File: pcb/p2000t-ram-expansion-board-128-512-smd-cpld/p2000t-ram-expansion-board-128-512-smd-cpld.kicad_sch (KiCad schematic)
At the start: 19 parts, among them J1 EXPANSION BOARD, J2 POWER, J3 TERMINAL, J4 Atmel-JTAG-10, U1 ATF1502ASV, U2 62128, U3 62128, U4 62128, U5 62128

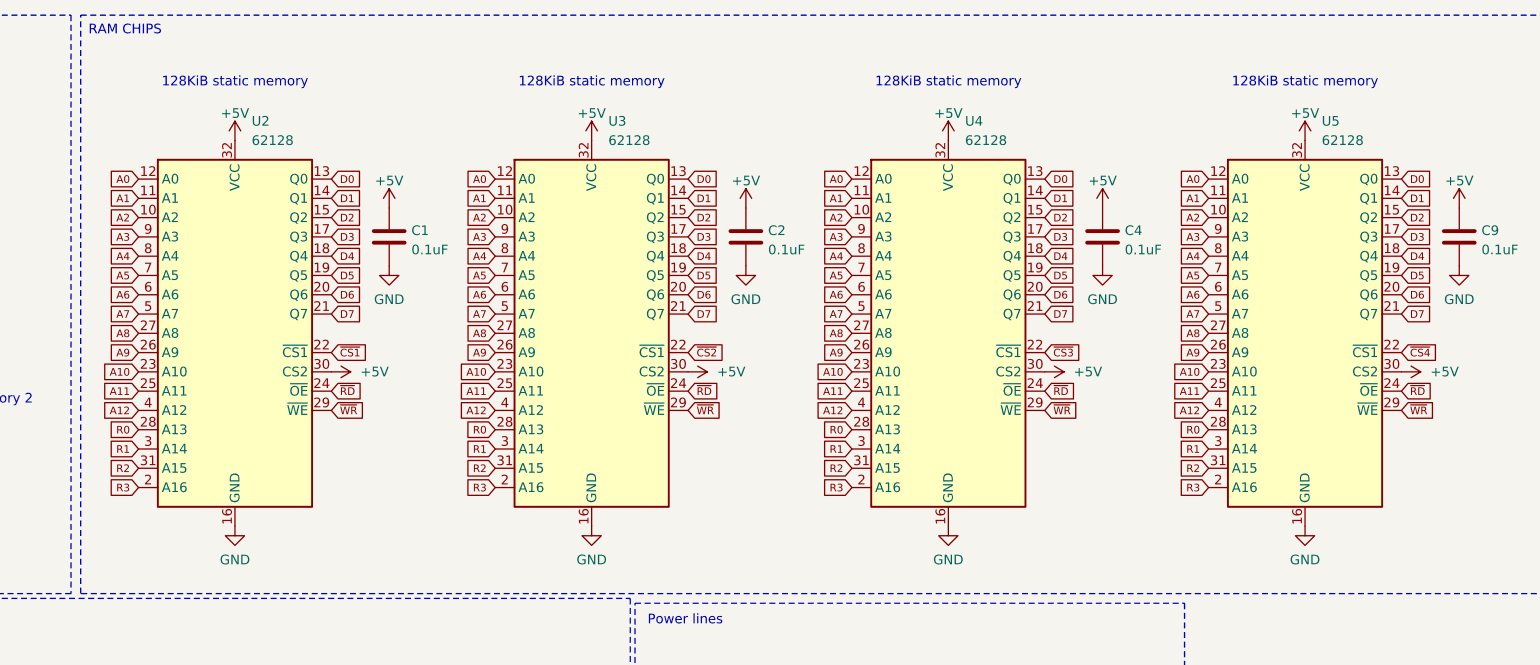
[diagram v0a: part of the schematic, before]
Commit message: Fixing CUPL code for multi-ram
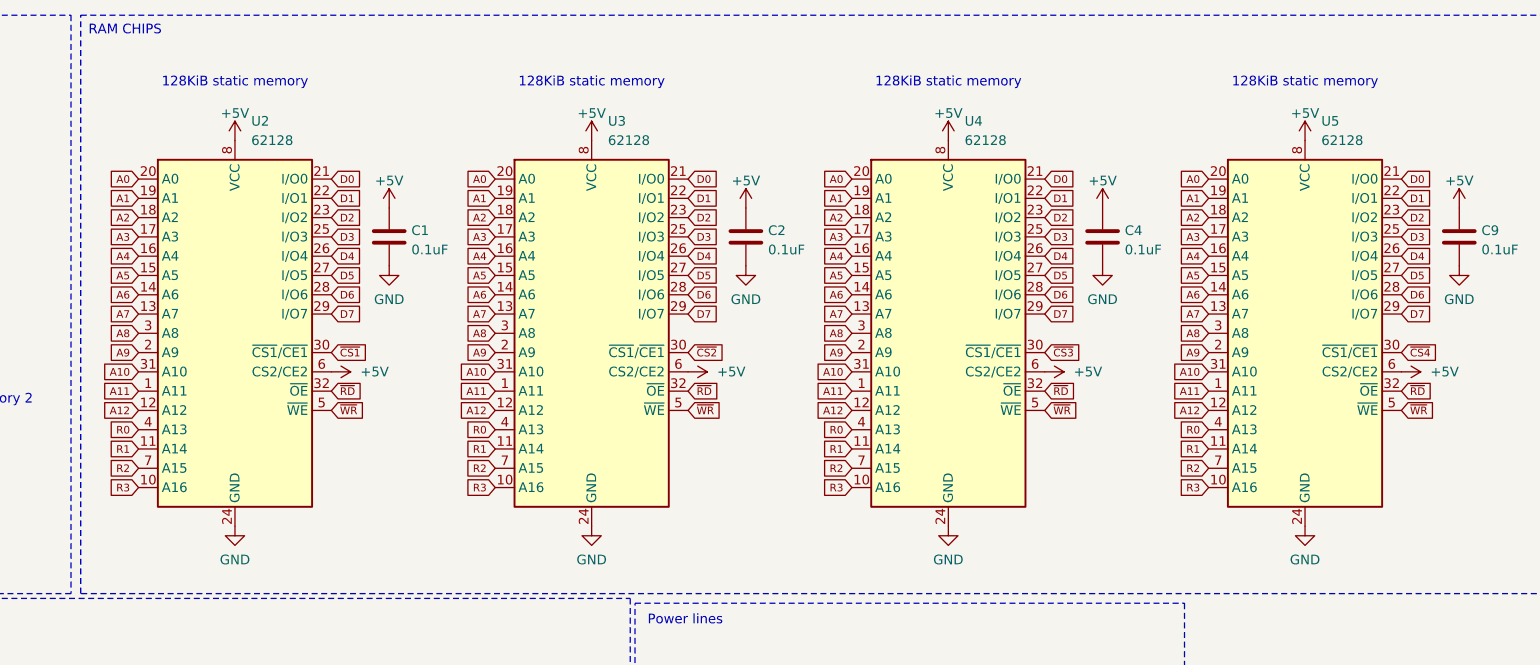
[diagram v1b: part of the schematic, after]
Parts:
- U2, U3, U4, U5: symbol Memory_RAM:628128_DIP32_SSOP32 -> Memory_RAM:CY62128Exx-xxZ
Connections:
- net +5V: now also U2.6 (CS2/CE2), U2.8 (VCC), U3.6 (CS2/CE2), U3.8 (VCC), U4.6 (CS2/CE2), U4.8 (VCC), U5.6 (CS2/CE2), U5.8 (VCC); no longer U2.30 (CS2), U2.32 (VCC), U3.30 (CS2), U3.32 (VCC), U4.30 (CS2), U4.32 (VCC), U5.30 (CS2), U5.32 (VCC)
- net A0: now also U2.20 (A0), U3.20 (A0), U4.20 (A0), U5.20 (A0); no longer U2.12 (A0), U3.12 (A0), U4.12 (A0), U5.12 (A0)
- net A1: now also U2.19 (A1), U3.19 (A1), U4.19 (A1), U5.19 (A1); no longer U2.11 (A1), U3.11 (A1), U4.11 (A1), U5.11 (A1)
- net A10: now also U2.31 (A10), U3.31 (A10), U4.31 (A10), U5.31 (A10); no longer U2.23 (A10), U3.23 (A10), U4.23 (A10), U5.23 (A10)
- net A11: now also U2.1 (A11), U3.1 (A11), U4.1 (A11), U5.1 (A11); no longer U2.25 (A11), U3.25 (A11), U4.25 (A11), U5.25 (A11)
- net A12: now also U2.12 (A12), U3.12 (A12), U4.12 (A12), U5.12 (A12); no longer U2.4 (A12), U3.4 (A12), U4.4 (A12), U5.4 (A12)
- net A2: now also U2.18 (A2), U3.18 (A2), U4.18 (A2), U5.18 (A2); no longer U2.10 (A2), U3.10 (A2), U4.10 (A2), U5.10 (A2)
- net A3: now also U2.17 (A3), U3.17 (A3), U4.17 (A3), U5.17 (A3); no longer U2.9 (A3), U3.9 (A3), U4.9 (A3), U5.9 (A3)
- net A4: now also U2.16 (A4), U3.16 (A4), U4.16 (A4), U5.16 (A4); no longer U2.8 (A4), U3.8 (A4), U4.8 (A4), U5.8 (A4)
- net A5: now also U2.15 (A5), U3.15 (A5), U4.15 (A5), U5.15 (A5); no longer U2.7 (A5), U3.7 (A5), U4.7 (A5), U5.7 (A5)
- net A6: now also U2.14 (A6), U3.14 (A6), U4.14 (A6), U5.14 (A6); no longer U2.6 (A6), U3.6 (A6), U4.6 (A6), U5.6 (A6)
- net A7: now also U2.13 (A7), U3.13 (A7), U4.13 (A7), U5.13 (A7); no longer U2.5 (A7), U3.5 (A7), U4.5 (A7), U5.5 (A7)
- net A8: now also U2.3 (A8), U3.3 (A8), U4.3 (A8), U5.3 (A8); no longer U2.27 (A8), U3.27 (A8), U4.27 (A8), U5.27 (A8)
- net A9: now also U2.2 (A9), U3.2 (A9), U4.2 (A9), U5.2 (A9); no longer U2.26 (A9), U3.26 (A9), U4.26 (A9), U5.26 (A9)
- net D0: now also U2.21 (I/O0), U3.21 (I/O0), U4.21 (I/O0), U5.21 (I/O0); no longer U2.13 (Q0), U3.13 (Q0), U4.13 (Q0), U5.13 (Q0)
- net D1: now also U2.22 (I/O1), U3.22 (I/O1), U4.22 (I/O1), U5.22 (I/O1); no longer U2.14 (Q1), U3.14 (Q1), U4.14 (Q1), U5.14 (Q1)
- net D2: now also U2.23 (I/O2), U3.23 (I/O2), U4.23 (I/O2), U5.23 (I/O2); no longer U2.15 (Q2), U3.15 (Q2), U4.15 (Q2), U5.15 (Q2)
- net D3: now also U2.25 (I/O3), U3.25 (I/O3), U4.25 (I/O3), U5.25 (I/O3); no longer U2.17 (Q3), U3.17 (Q3), U4.17 (Q3), U5.17 (Q3)
- net D4: now also U2.26 (I/O4), U3.26 (I/O4), U4.26 (I/O4), U5.26 (I/O4); no longer U2.18 (Q4), U3.18 (Q4), U4.18 (Q4), U5.18 (Q4)
- net D5: now also U2.27 (I/O5), U3.27 (I/O5), U4.27 (I/O5), U5.27 (I/O5); no longer U2.19 (Q5), U3.19 (Q5), U4.19 (Q5), U5.19 (Q5)
- net D6: now also U2.28 (I/O6), U3.28 (I/O6), U4.28 (I/O6), U5.28 (I/O6); no longer U2.20 (Q6), U3.20 (Q6), U4.20 (Q6), U5.20 (Q6)
- net D7: now also U2.29 (I/O7), U3.29 (I/O7), U4.29 (I/O7), U5.29 (I/O7); no longer U2.21 (Q7), U3.21 (Q7), U4.21 (Q7), U5.21 (Q7)
- net GND: now also U2.24 (GND), U3.24 (GND), U4.24 (GND), U5.24 (GND); no longer U2.16 (GND), U3.16 (GND), U4.16 (GND), U5.16 (GND)
- net R0: now also U2.4 (A13), U3.4 (A13), U4.4 (A13), U5.4 (A13); no longer U2.28 (A13), U3.28 (A13), U4.28 (A13), U5.28 (A13)
- net R1: now also U2.11 (A14), U3.11 (A14), U4.11 (A14), U5.11 (A14); no longer U2.3 (A14), U3.3 (A14), U4.3 (A14), U5.3 (A14)
- net R2: now also U2.7 (A15), U3.7 (A15), U4.7 (A15), U5.7 (A15); no longer U2.31 (A15), U3.31 (A15), U4.31 (A15), U5.31 (A15)
- net R3: now also U2.10 (A16), U3.10 (A16), U4.10 (A16), U5.10 (A16); no longer U2.2 (A16), U3.2 (A16), U4.2 (A16), U5.2 (A16)
- net ~{CS1}: now also U2.30 (~{CS1}/~{CE1}); no longer U2.22 (~{CS1})
- net ~{CS2}: now also U3.30 (~{CS1}/~{CE1}); no longer U3.22 (~{CS1})
- net ~{CS3}: now also U4.30 (~{CS1}/~{CE1}); no longer U4.22 (~{CS1})
- net ~{CS4}: now also U5.30 (~{CS1}/~{CE1}); no longer U5.22 (~{CS1})
- net ~{RD}: now also U2.32 (~{OE}), U3.32 (~{OE}), U4.32 (~{OE}), U5.32 (~{OE}); no longer U2.24 (~{OE}), U3.24 (~{OE}), U4.24 (~{OE}), U5.24 (~{OE})
- net ~{WR}: now also U2.5 (~{WE}), U3.5 (~{WE}), U4.5 (~{WE}), U5.5 (~{WE}); no longer U2.29 (~{WE}), U3.29 (~{WE}), U4.29 (~{WE}), U5.29 (~{WE})
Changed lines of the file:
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@@
 	)
 	(symbol
-		(lib_id "Memory_RAM:628128_DIP32_SSOP32")
+		(lib_id "Memory_RAM:CY62128Exx-xxZ")
 		(at 241.3 54.61 0)
 		(unit 1)
@@
 		(fields_autoplaced yes)
 		(property "Reference" "U5"
-			(at 243.4941 26.67 0)
+			(at 243.4433 26.67 0)
 			(effects
 				(font
@@
 		)
 		(property "Value" "62128"
-			(at 243.4941 29.21 0)
+			(at 243.4433 29.21 0)
 			(effects
 				(font
@@
 			)
 		)
-		(property "Datasheet" "http://www.futurlec.com/Datasheet/Memory/628128.pdf"
+		(property "Datasheet" "https://www.infineon.com/dgdl/Infineon-CY62128E_MoBL_1-Mbit_(128_K_8)_Static_RAM-DataSheet-v17_00-EN.pdf?fileId=8ac78c8c7d0d8da4017d0ebe7dc7321d"
 			(at 241.3 54.61 0)
 			(effects
@@
 			)
 		)
-		(property "Description" "128K x 8 High-Speed CMOS Static RAM, 55/70ns, DIP-32/SSOP-32"
+		(property "Description" "1-Mbit (128K x 8-bit) Static RAM, VCC = 4.5..5.5V, 45/55ns, TSOP-I-32"
 			(at 241.3 54.61 0)
 			(effects
@@
 		(pin "8"
 		)
+		(pin "27"
+		)
 		(pin "9"
-		)
-		(pin "27"
 		)
 		(instances
@@
 	)
 	(symbol
-		(lib_id "Memory_RAM:628128_DIP32_SSOP32")
+		(lib_id "Memory_RAM:CY62128Exx-xxZ")
 		(at 147.32 54.61 0)
 		(unit 1)
@@
 		(fields_autoplaced yes)
 		(property "Reference" "U3"
-			(at 149.5141 26.67 0)
+			(at 149.4633 26.67 0)
 			(effects
 				(font
@@
 		)
 		(property "Value" "62128"
-			(at 149.5141 29.21 0)
+			(at 149.4633 29.21 0)
 			(effects
 				(font
@@
 			)
 		)
-		(property "Datasheet" "http://www.futurlec.com/Datasheet/Memory/628128.pdf"
+		(property "Datasheet" "https://www.infineon.com/dgdl/Infineon-CY62128E_MoBL_1-Mbit_(128_K_8)_Static_RAM-DataSheet-v17_00-EN.pdf?fileId=8ac78c8c7d0d8da4017d0ebe7dc7321d"
 			(at 147.32 54.61 0)
 			(effects
@@
 			)
 		)
-		(property "Description" "128K x 8 High-Speed CMOS Static RAM, 55/70ns, DIP-32/SSOP-32"
+		(property "Description" "1-Mbit (128K x 8-bit) Static RAM, VCC = 4.5..5.5V, 45/55ns, TSOP-I-32"
 			(at 147.32 54.61 0)
 			(effects
@@
 		(pin "8"
 		)
+		(pin "27"
+		)
 		(pin "9"
-		)
-		(pin "27"
 		)
 		(instances
@@
 	)
 	(symbol
-		(lib_id "Memory_RAM:628128_DIP32_SSOP32")
+		(lib_id "Memory_RAM:CY62128Exx-xxZ")
 		(at 100.33 54.61 0)
 		(unit 1)
@@
 		(fields_autoplaced yes)
 		(property "Reference" "U2"
-			(at 102.5241 26.67 0)
+			(at 102.4733 26.67 0)
 			(effects
 				(font
@@
 		)
 		(property "Value" "62128"
-			(at 102.5241 29.21 0)
+			(at 102.4733 29.21 0)
 			(effects
 				(font
@@
 			)
 		)
-		(property "Datasheet" "http://www.futurlec.com/Datasheet/Memory/628128.pdf"
+		(property "Datasheet" "https://www.infineon.com/dgdl/Infineon-CY62128E_MoBL_1-Mbit_(128_K_8)_Static_RAM-DataSheet-v17_00-EN.pdf?fileId=8ac78c8c7d0d8da4017d0ebe7dc7321d"
 			(at 100.33 54.61 0)
 			(effects
@@
 			)
 		)
-		(property "Description" "128K x 8 High-Speed CMOS Static RAM, 55/70ns, DIP-32/SSOP-32"
+		(property "Description" "1-Mbit (128K x 8-bit) Static RAM, VCC = 4.5..5.5V, 45/55ns, TSOP-I-32"
 			(at 100.33 54.61 0)
 			(effects
@@
 		(pin "2"
 		)
+		(pin "14"
+		)
+		(pin "19"
+		)
+		(pin "32"
+		)
+		(pin "4"
+		)
+		(pin "23"
+		)
+		(pin "24"
+		)
+		(pin "7"
+		)
+		(pin "29"
+		)
+		(pin "16"
+		)
+		(pin "25"
+		)
+		(pin "28"
+		)
+		(pin "11"
+		)
+		(pin "30"
+		)
+		(pin "12"
+		)
+		(pin "18"
+		)
+		(pin "6"
+		)
+		(pin "17"
+		)
+		(pin "21"
+		)
+		(pin "22"
+		)
+		(pin "26"
+		)
+		(pin "3"
+		)
+		(pin "27"
+		)
+		(pin "1"
+		)
+		(pin "31"
+		)
 		(pin "10"
 		)
-		(pin "19"
-		)
-		(pin "32"
-		)
-		(pin "14"
-		)
-		(pin "23"
-		)
-		(pin "24"
-		)
 		(pin "13"
 		)
-		(pin "29"
-		)
-		(pin "16"
-		)
-		(pin "25"
-		)
-		(pin "28"
-		)
-		(pin "3"
-		)
-		(pin "30"
-		)
-		(pin "4"
-		)
-		(pin "18"
-		)
 		(pin "15"
 		)
-		(pin "11"
-		)
-		(pin "21"
-		)
-		(pin "22"
-		)
-		(pin "26"
+		(pin "8"
 		)
 		(pin "5"
 		)
-		(pin "7"
-		)
-		(pin "17"
-		)
-		(pin "31"
-		)
-		(pin "1"
-		)
-		(pin "12"
-		)
-		(pin "6"
-		)
-		(pin "8"
-		)
 		(pin "9"
-		)
-		(pin "27"
 		)
 		(instances
@@
 	)
 	(symbol
-		(lib_id "Memory_RAM:628128_DIP32_SSOP32")
+		(lib_id "Memory_RAM:CY62128Exx-xxZ")
 		(at 194.31 54.61 0)
 		(unit 1)
@@
 		(fields_autoplaced yes)
 		(property "Reference" "U4"
-			(at 196.5041 26.67 0)
+			(at 196.4533 26.67 0)
 			(effects
 				(font
@@
 		)
 		(property "Value" "62128"
-			(at 196.5041 29.21 0)
+			(at 196.4533 29.21 0)
 			(effects
 				(font
@@
 			)
 		)
-		(property "Datasheet" "http://www.futurlec.com/Datasheet/Memory/628128.pdf"
+		(property "Datasheet" "https://www.infineon.com/dgdl/Infineon-CY62128E_MoBL_1-Mbit_(128_K_8)_Static_RAM-DataSheet-v17_00-EN.pdf?fileId=8ac78c8c7d0d8da4017d0ebe7dc7321d"
 			(at 194.31 54.61 0)
 			(effects
@@
 			)
 		)
-		(property "Description" "128K x 8 High-Speed CMOS Static RAM, 55/70ns, DIP-32/SSOP-32"
+		(property "Description" "1-Mbit (128K x 8-bit) Static RAM, VCC = 4.5..5.5V, 45/55ns, TSOP-I-32"
 			(at 194.31 54.61 0)
 			(effects
@@
 		(pin "8"
 		)
+		(pin "27"
+		)
 		(pin "9"
 		)
-		(pin "27"
-		)
-		(instances
+		(instances
